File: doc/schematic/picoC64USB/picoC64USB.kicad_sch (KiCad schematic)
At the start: 5 parts, among them J1 DB9_Female, U1 Pico, U2 PC847, U3 PC817

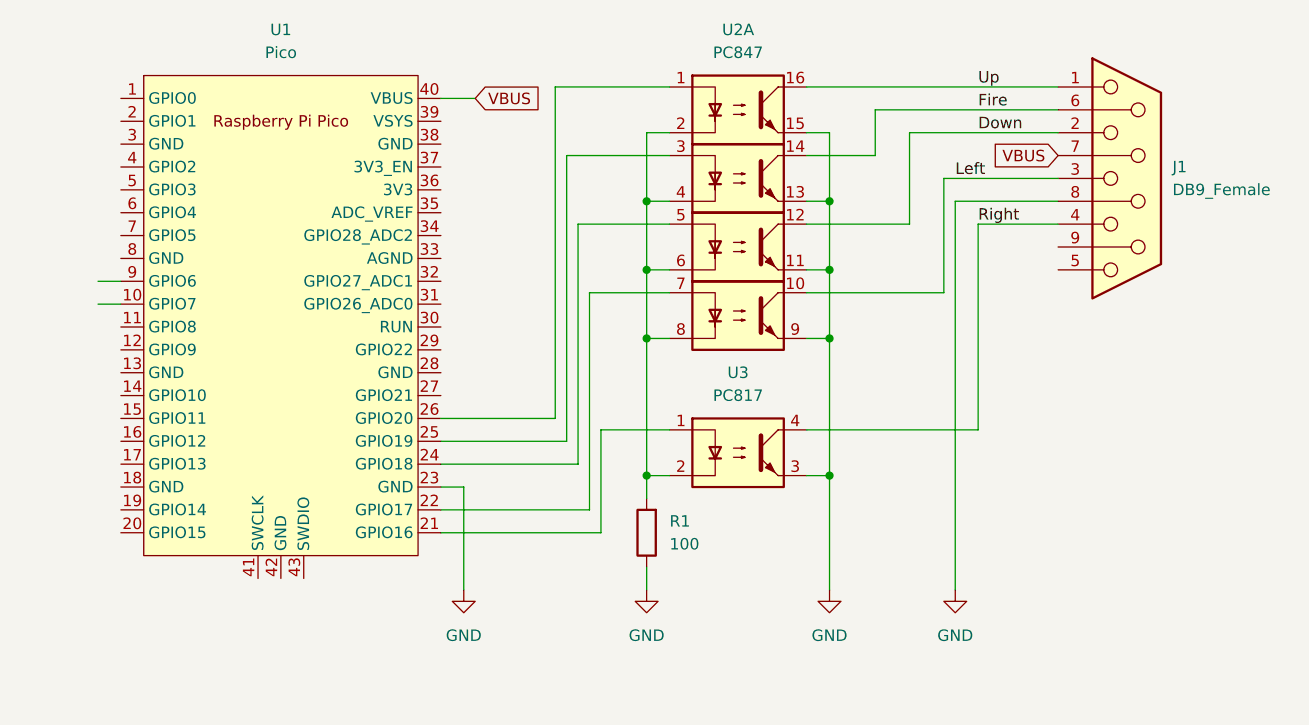
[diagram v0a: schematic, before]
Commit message: Changed schematic: one Resistor per channel
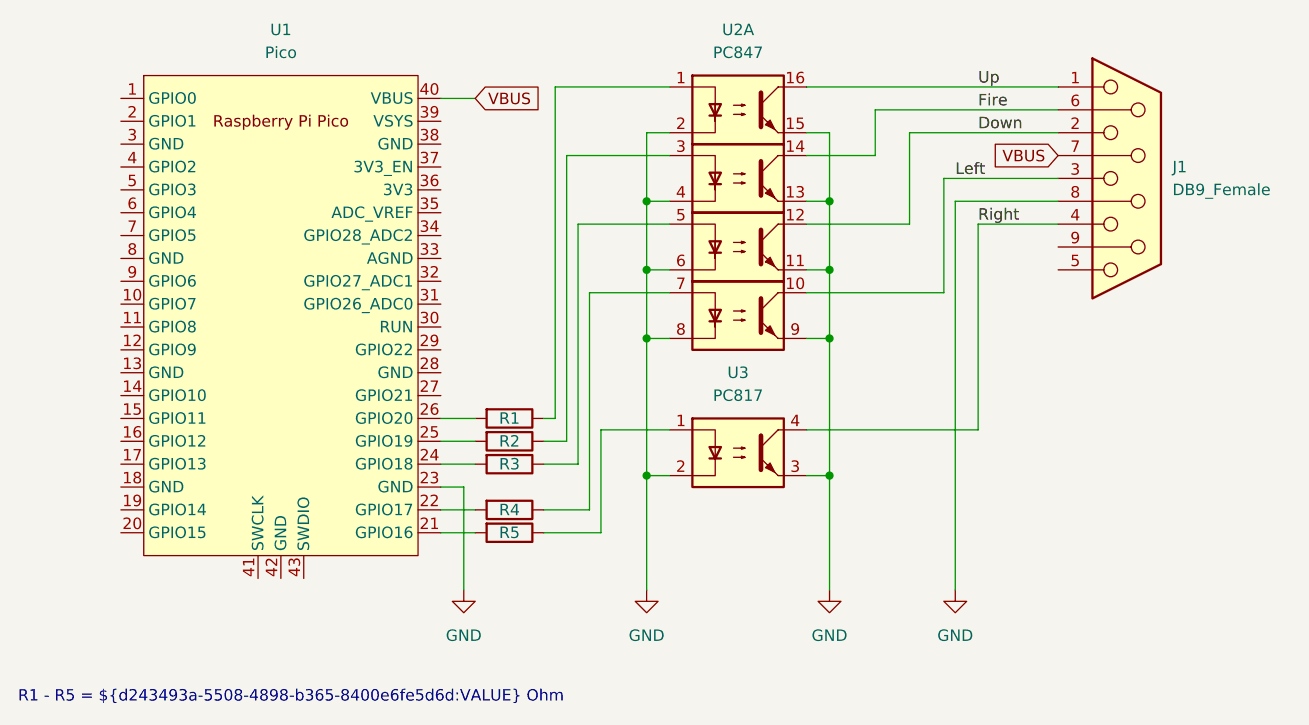
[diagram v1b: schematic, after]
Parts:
- added R2: ${d243493a-5508-4898-b365-8400e6fe5d6d:VALUE}, symbol Device:R
- added R3, R4, R5: ${R1:VALUE}, symbol Device:R
- R1: value 100 -> 200
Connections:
- net GND: now also U2.2, U2.4, U2.6, U2.8, U3.2; no longer R1.1
- net at U3.1: now also R5.1; no longer U1.21 (GPIO16)
- net at U2.7: now also R4.1; no longer U1.22 (GPIO17)
- net at U2.5: now also R3.1; no longer U1.24 (GPIO18)
- net at U2.3: now also R2.1; no longer U1.25 (GPIO19)
- net at U1.26 (GPIO20): now also R1.2; no longer U2.1
- new net: R5.2, U1.21 (GPIO16)
- new net: R2.2, U1.25 (GPIO19)
- new net: R4.2, U1.22 (GPIO17)
- new net: R3.2, U1.24 (GPIO18)
- new net: R1.1, U2.1
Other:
- note added: "R1 - R5 = ${d243493a-5508-4898-b365-8400e6fe5d6d:VALUE} Ohm"
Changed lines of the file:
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@@
   (junction (at 105.41 41.91) (diameter 0) (color 0 0 0 0)
   )
-  (wire (pts (xy 80.01 71.12) (xy 62.23 71.12))
+  (wire (pts (xy 80.01 71.12) (xy 73.66 71.12))
     (stroke (width 0) (type default) (color 0 0 0 0))
   )
@@
     (stroke (width 0) (type default) (color 0 0 0 0))
   )
-  (wire (pts (xy 74.93 58.42) (xy 62.23 58.42))
+  (wire (pts (xy 73.66 68.58) (xy 78.74 68.58))
+    (stroke (width 0) (type default) (color 0 0 0 0))
+  )
+  (wire (pts (xy 74.93 58.42) (xy 73.66 58.42))
+    (stroke (width 0) (type default) (color 0 0 0 0))
+  )
+  (wire (pts (xy 66.04 58.42) (xy 62.23 58.42))
     (stroke (width 0) (type default) (color 0 0 0 0))
   )
@@
     (stroke (width 0) (type default) (color 0 0 0 0))
   )
+  (wire (pts (xy 66.04 63.5) (xy 62.23 63.5))
+    (stroke (width 0) (type default) (color 0 0 0 0))
+  )
   (wire (pts (xy 118.11 31.75) (xy 118.11 44.45))
     (stroke (width 0) (type default) (color 0 0 0 0))
@@
     (stroke (width 0) (type default) (color 0 0 0 0))
   )
-  (wire (pts (xy 24.13 45.72) (xy 26.67 45.72))
-    (stroke (width 0) (type default) (color 0 0 0 0))
-  )
   (wire (pts (xy 102.87 34.29) (xy 105.41 34.29))
     (stroke (width 0) (type default) (color 0 0 0 0))
@@
     (stroke (width 0) (type default) (color 0 0 0 0))
   )
-  (wire (pts (xy 62.23 68.58) (xy 78.74 68.58))
-    (stroke (width 0) (type default) (color 0 0 0 0))
-  )
-  (wire (pts (xy 76.2 60.96) (xy 62.23 60.96))
+  (wire (pts (xy 66.04 60.96) (xy 62.23 60.96))
+    (stroke (width 0) (type default) (color 0 0 0 0))
+  )
+  (wire (pts (xy 62.23 68.58) (xy 66.04 68.58))
+    (stroke (width 0) (type default) (color 0 0 0 0))
+  )
+  (wire (pts (xy 76.2 60.96) (xy 73.66 60.96))
     (stroke (width 0) (type default) (color 0 0 0 0))
   )
@@
     (stroke (width 0) (type default) (color 0 0 0 0))
   )
+  (wire (pts (xy 66.04 71.12) (xy 62.23 71.12))
+    (stroke (width 0) (type default) (color 0 0 0 0))
+  )
   (wire (pts (xy 119.38 34.29) (xy 119.38 77.47))
     (stroke (width 0) (type default) (color 0 0 0 0))
@@
     (stroke (width 0) (type default) (color 0 0 0 0))
   )
-  (wire (pts (xy 77.47 63.5) (xy 62.23 63.5))
+  (wire (pts (xy 77.47 63.5) (xy 73.66 63.5))
     (stroke (width 0) (type default) (color 0 0 0 0))
   )
@@
     (stroke (width 0) (type default) (color 0 0 0 0))
   )
-  (wire (pts (xy 85.09 74.93) (xy 85.09 77.47))
-    (stroke (width 0) (type default) (color 0 0 0 0))
-  )
-  (wire (pts (xy 85.09 64.77) (xy 85.09 67.31))
+  (wire (pts (xy 85.09 64.77) (xy 85.09 77.47))
     (stroke (width 0) (type default) (color 0 0 0 0))
   )
@@
     (stroke (width 0) (type default) (color 0 0 0 0))
   )
-  (wire (pts (xy 24.13 43.18) (xy 26.67 43.18))
-    (stroke (width 0) (type default) (color 0 0 0 0))
-  )
   (wire (pts (xy 102.87 21.59) (xy 130.81 21.59))
     (stroke (width 0) (type default) (color 0 0 0 0))
@@
   (wire (pts (xy 102.87 41.91) (xy 105.41 41.91))
     (stroke (width 0) (type default) (color 0 0 0 0))
+  )
+  (text "R1 - R5 = ${d243493a-5508-4898-b365-8400e6fe5d6d:VALUE} Ohm"
+    (at 15.24 90.17 0)
+    (effects (font (size 1.27 1.27)) (justify left bottom))
   )
   (label "Right" (at 121.92 36.83 0)
@@
     (pin "1")
   )
-  (symbol (lib_id "Device:R") (at 85.09 71.12 180) (unit 1)
-    (in_bom yes) (on_board yes) (fields_autoplaced)
-    (property "Reference" "R1" (id 0) (at 87.63 69.8499 0)
-      (effects (font (size 1.27 1.27)) (justify right))
-    )
-    (property "Value" "100" (id 1) (at 87.63 72.3899 0)
-      (effects (font (size 1.27 1.27)) (justify right))
-    )
-    (property "Footprint" "" (id 2) (at 86.868 71.12 90)
-      (effects (font (size 1.27 1.27)) hide)
-    )
-    (property "Datasheet" "~" (id 3) (at 85.09 71.12 0)
+  (symbol (lib_id "Device:R") (at 69.85 71.12 270) (unit 1)
+    (in_bom yes) (on_board yes)
+    (property "Reference" "R5" (id 0) (at 69.85 71.12 90))
+    (property "Value" "${R1:VALUE}" (id 1) (at 69.85 67.31 90)
+      (effects (font (size 1.27 1.27)) hide)
+    )
+    (property "Footprint" "" (id 2) (at 69.85 69.342 90)
+      (effects (font (size 1.27 1.27)) hide)
+    )
+    (property "Datasheet" "~" (id 3) (at 69.85 71.12 0)
+      (effects (font (size 1.27 1.27)) hide)
+    )
+    (pin "1")
+    (pin "2")
+  )
+  (symbol (lib_id "Device:R") (at 69.85 60.96 270) (unit 1)
+    (in_bom yes) (on_board yes)
+    (property "Reference" "R2" (id 0) (at 69.85 60.96 90))
+    (property "Value" "${d243493a-5508-4898-b365-8400e6fe5d6d:VALUE}" (id 1) (at 69.85 57.15 90)
+      (effects (font (size 1.27 1.27)) hide)
+    )
+    (property "Footprint" "" (id 2) (at 69.85 59.182 90)
+      (effects (font (size 1.27 1.27)) hide)
+    )
+    (property "Datasheet" "~" (id 3) (at 69.85 60.96 0)
       (effects (font (size 1.27 1.27)) hide)
     )
@@
     (pin "8")
     (pin "9")
+  )
+  (symbol (lib_id "Device:R") (at 69.85 68.58 270) (unit 1)
+    (in_bom yes) (on_board yes)
+    (property "Reference" "R4" (id 0) (at 69.85 68.58 90))
+    (property "Value" "${R1:VALUE}" (id 1) (at 69.85 64.77 90)
+      (effects (font (size 1.27 1.27)) hide)
+    )
+    (property "Footprint" "" (id 2) (at 69.85 66.802 90)
+      (effects (font (size 1.27 1.27)) hide)
+    )
+    (property "Datasheet" "~" (id 3) (at 69.85 68.58 0)
+      (effects (font (size 1.27 1.27)) hide)
+    )
+    (pin "1")
+    (pin "2")
+  )
+  (symbol (lib_id "Device:R") (at 69.85 63.5 270) (unit 1)
+    (in_bom yes) (on_board yes)
+    (property "Reference" "R3" (id 0) (at 69.85 63.5 90))
+    (property "Value" "${R1:VALUE}" (id 1) (at 69.85 59.69 90)
+      (effects (font (size 1.27 1.27)) hide)
+    )
+    (property "Footprint" "" (id 2) (at 69.85 61.722 90)
+      (effects (font (size 1.27 1.27)) hide)
+    )
+    (property "Datasheet" "~" (id 3) (at 69.85 63.5 0)
+      (effects (font (size 1.27 1.27)) hide)
+    )
+    (pin "1")
+    (pin "2")
   )
   (symbol (lib_id "Isolator:PC847") (at 95.25 39.37 0) (unit 3)
@@
     (pin "9")
   )
+  (symbol (lib_id "Device:R") (at 69.85 58.42 270) (unit 1)
+    (in_bom yes) (on_board yes)
+    (property "Reference" "R1" (id 0) (at 69.85 58.42 90))
+    (property "Value" "200" (id 1) (at 69.85 49.53 90)
+      (effects (font (size 1.27 1.27)) hide)
+    )
+    (property "Footprint" "" (id 2) (at 69.85 56.642 90)
+      (effects (font (size 1.27 1.27)) hide)
+    )
+    (property "Datasheet" "~" (id 3) (at 69.85 58.42 0)
+      (effects (font (size 1.27 1.27)) hide)
+    )
+    (pin "1")
+    (pin "2")
+  )
   (symbol (lib_id "Isolator:PC847") (at 95.25 24.13 0) (unit 1)
     (in_bom yes) (on_board yes) (fields_autoplaced)
@@
       (reference "J1") (unit 1) (value "DB9_Female") (footprint "Connector_Dsub:DSUB-9_Female_EdgeMount_P2.77mm")
     )
-    (path "/6001dddb-c7e6-4868-b49d-c88e019afcf2"
-      (reference "R1") (unit 1) (value "100") (footprint "")
+    (path "/d243493a-5508-4898-b365-8400e6fe5d6d"
+      (reference "R1") (unit 1) (value "200") (footprint "")
+    )
+    (path "/4c9a0747-e230-4c06-99fb-fcfb6ebc09d2"
+      (reference "R2") (unit 1) (value "${d243493a-5508-4898-b365-8400e6fe5d6d:VALUE}") (footprint "")
+    )
+    (path "/73e54148-4400-4e8c-b815-a49304448a73"
+      (reference "R3") (unit 1) (value "${R1:VALUE}") (footprint "")
+    )
+    (path "/6da25e28-86ff-4035-89e2-4b02f09d819e"
+      (reference "R4") (unit 1) (value "${R1:VALUE}") (footprint "")
+    )
+    (path "/471d8cbe-fe9c-47d6-87f8-6d84a07deea8"
+      (reference "R5") (unit 1) (value "${R1:VALUE}") (footprint "")
     )
     (path "/c193e54f-36f1-43b3-bb9f-fb59aa0a3b7f"
